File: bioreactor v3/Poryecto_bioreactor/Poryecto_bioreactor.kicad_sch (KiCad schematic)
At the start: 11 parts, among them J1 Screw_Terminal_01x02, U2 OKI-78SR-5/1.5-W36-C (L7805)

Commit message: Actualizacion
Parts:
- added C11: 100 nF, symbol Device:C
- added D2: 1N5819, Diode_THT:D_DO-41_SOD81_P10.16mm_Horizontal, symbol Diode:1N5819
- added J_BTN_NAV, J_BTN_ON, J_BTN_REG, J_BTN_RESET, J_MOTOR: PinHeader_1x02_P2.54mm_Vertical, symbol Connector_Generic:Conn_01x02
- added J_LCD: Conn_01x04_Pin, Connector_PinHeader_2.54mm:PinHeader_1x04_P2.54mm_Vertical, symbol Connector:Conn_01x04_Pin
- added J_RPM, J_TEMP: Conn_01x03, Connector_PinHeader_2.54mm:PinHeader_1x03_P2.54mm_Vertical, symbol Connector_Generic:Conn_01x03
- added Q1: IRLZ44N, Package_TO_SOT_THT:TO-220-3_Vertical, symbol Transistor_FET:IRLZ44N
- added R4: 10 kΩ, Package_TO_SOT_THT:TO-220-3_Vertical, symbol Device:R
- added R5: 4,7 kΩ, symbol Device:R
- added R6: 10 kΩ, symbol Device:R
- added R7: R, symbol Device:R
- R3: renamed from R1; value R -> 100 Ω
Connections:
- net +12V_PROT: now also C11.2, D2.1 (K), J_MOTOR.1 (Pin_1)
- net +5V: now also J_RPM.1 (Pin_1), J_TEMP.1 (Pin_1), R5.2, R6.2
- net GND: now also J_RPM.3 (Pin_3), J_TEMP.3 (Pin_3), Q1.3 (S), R4.1
- net BTN_NAV: now reaches A1.10 (D7)
- net BTN_NAV: now also J_BTN_NAV.1 (Pin_1)
- net ALARM_CTRL: now reaches A1.11 (D8)
- net ALARM_CTRL: now also R7.1
- net PWM_MOTOR: now reaches A1.12 (D9)
- net PWM_MOTOR: now also R3.1
- net SDA: now reaches A1.23 (A4)
- net SDA: now also J_LCD.3 (Pin_3)
- net SCL: now reaches A1.24 (A5)
- net SCL: now also J_LCD.4 (Pin_4)
- net RESET: now reaches A1.28 (~{RESET})
- net RESET: now also A1.3 (~{RESET}), J_BTN_RESET.1 (Pin_1)
- net RPM_SIGNAL: now reaches A1.5 (D2)
- net RPM_SIGNAL: now also J_RPM.2 (Pin_2), R6.1
- net TEMP_DATA: now reaches A1.7 (D4)
- net TEMP_DATA: now also J_TEMP.2 (Pin_2), R5.1
- net BTN_ON: now reaches A1.8 (D5)
- net BTN_ON: now also J_BTN_ON.1 (Pin_1)
- net BTN_REG: now reaches A1.9 (D6)
- net BTN_REG: now also J_BTN_REG.1 (Pin_1)
- net GATE_Q1: now reaches R3.2
- net GATE_Q1: now also Q1.1 (G), R4.2
- new net MOTOR-: C11.1, D2.2 (A), J_MOTOR.2 (Pin_2), Q1.2 (D)
- no-connect marks 3 -> 14
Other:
- note added: "18"
- note added: "19"
- note added: "20"
- note added: "21"
- note added: "22"
- note added: "23"
- note added: "24"
- note added: "25"
- note added: "26"
- note added: "27"
- note added: "28"
- note added: "29"
- note added: "30"
- note added: "31"
- note added: "32"
- note added: "33"
- note added: "34"
- note added: "35"
- note added: "36"
- note added: "37"
- note added: "38"
- note added: "39"
- note added: "Conector (bornera) para el sensor RPM"
- note added: "Conector (bornera) para el sensor de temperatura"
- note added: "Conector (bornera) para la pantalla"
- note added: "Conector para el botón de encendido"
- note added: "Todos los pines marcados con x no se ocuparán"
- note added: "conector del motor de 6 V"
- note removed: "VIN, 3V3, AREF no se usarán"
- moved on the sheet: R3

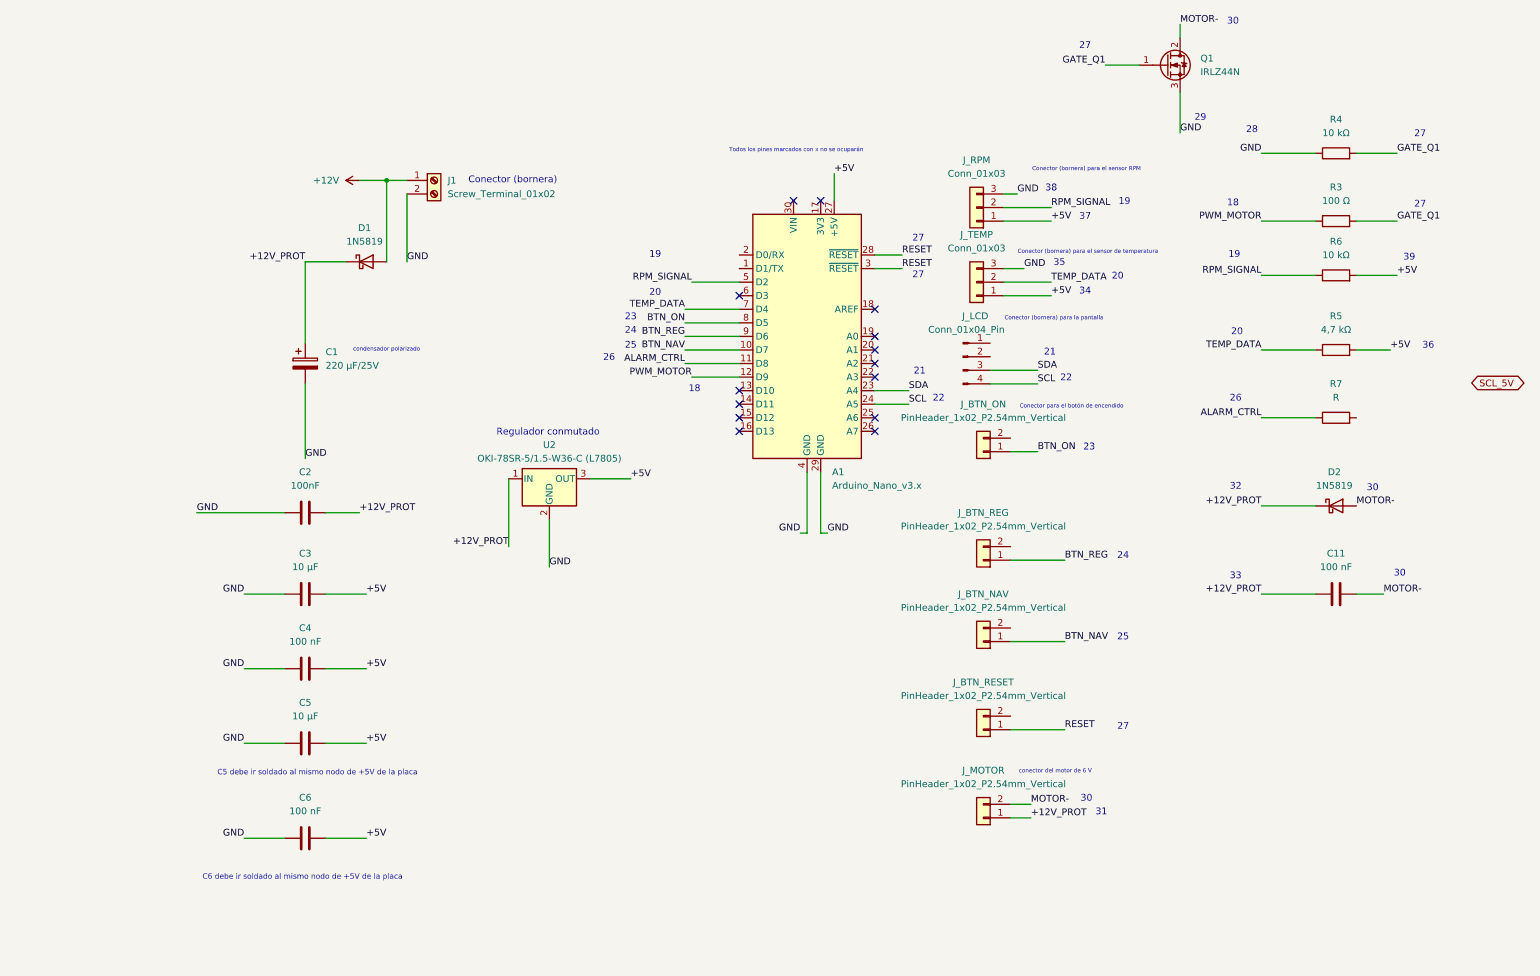
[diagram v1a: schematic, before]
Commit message: Esquemático terminado, generado de lista de componentes boom
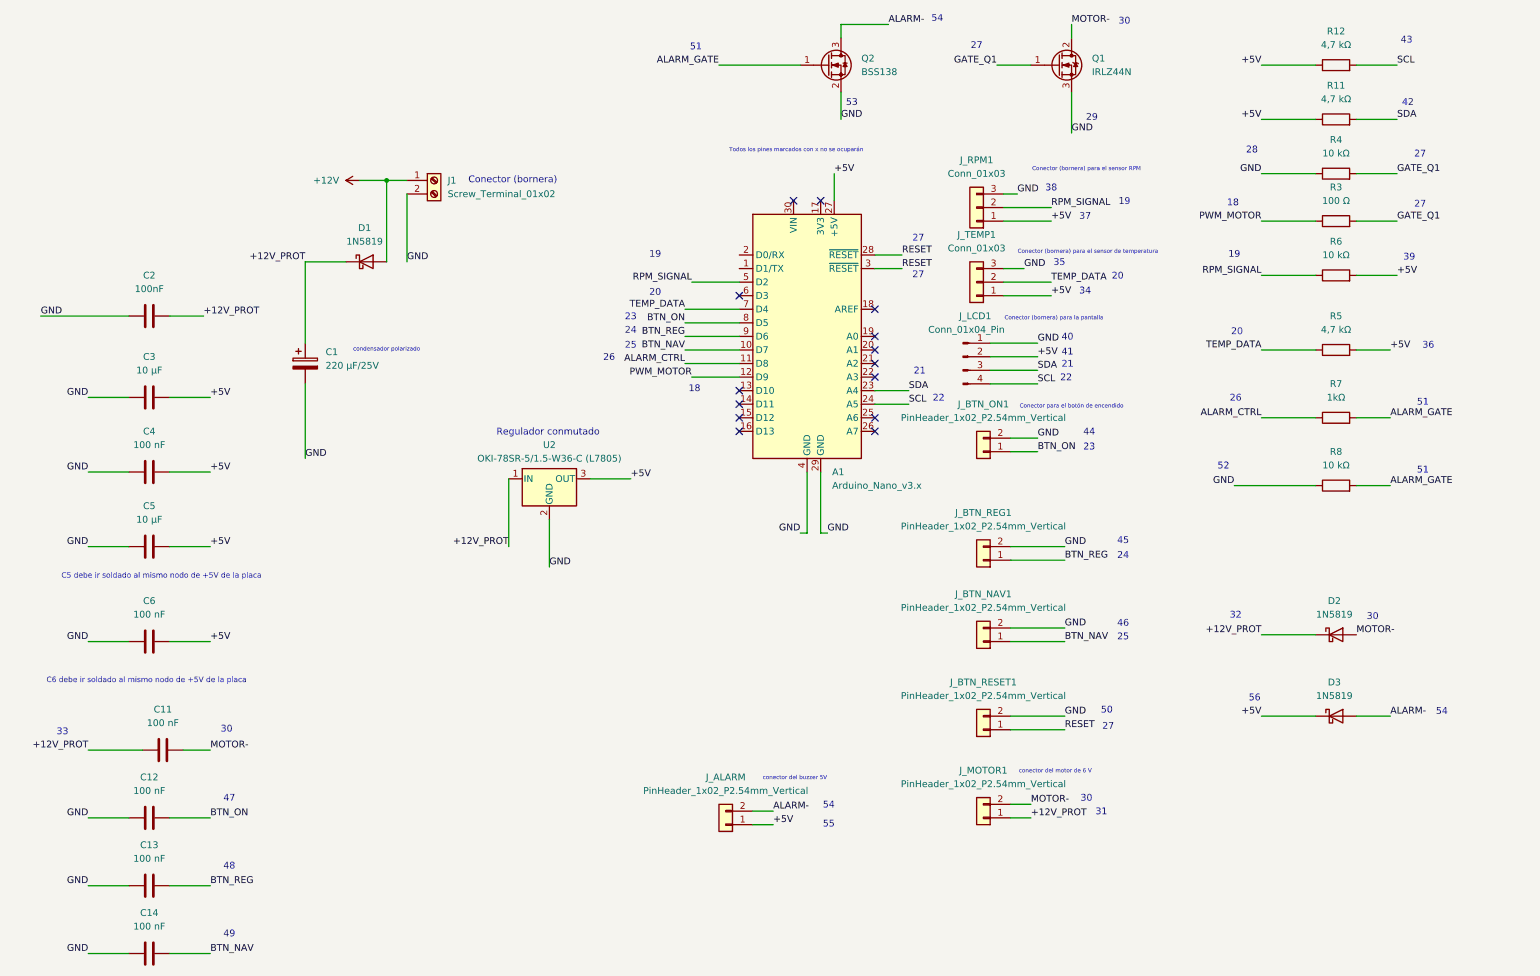
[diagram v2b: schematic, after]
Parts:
- added C12, C13, C14: 100 nF, symbol Device:C
- added D3: 1N5819, Diode_THT:D_DO-41_SOD81_P10.16mm_Horizontal, symbol Diode:1N5819
- added J_ALARM: PinHeader_1x02_P2.54mm_Vertical, symbol Connector_Generic:Conn_01x02
- added Q2: BSS138, Package_TO_SOT_SMD:SOT-23, symbol Transistor_FET:BSS138
- added R11, R12: 4,7 kΩ, Package_TO_SOT_THT:TO-220-3_Vertical, symbol Device:R
- added R8: 10 kΩ, symbol Device:R
- R7: value R -> 1kΩ
- renumbered J_BTN_NAV to J_BTN_NAV1, J_BTN_ON to J_BTN_ON1, J_BTN_REG to J_BTN_REG1, J_BTN_RESET to J_BTN_RESET1, J_LCD to J_LCD1, J_MOTOR to J_MOTOR1, J_RPM to J_RPM1, J_TEMP to J_TEMP1
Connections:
- net +5V: now also J_LCD1.2 (Pin_2), D3.1 (K), J_ALARM.1 (Pin_1), R11.1, R12.1
- net BTN_ON: now also C12.1
- net GND: now also J_BTN_NAV1.2 (Pin_2), J_BTN_ON1.2 (Pin_2), J_BTN_REG1.2 (Pin_2), J_BTN_RESET1.2 (Pin_2), J_LCD1.1 (Pin_1), C12.2, C13.2, C14.2, Q2.2 (S), R8.1
- net SCL: now also R12.2
- net SDA: now also R11.2
- net ALARM_GATE: now reaches R7.2
- net ALARM_GATE: now also Q2.1 (G), R8.2
- new net ALARM-: D3.2 (A), J_ALARM.2 (Pin_2), Q2.3 (D)
- new net BTN_NAV : C14.1
- new net BTN_REG : C13.1
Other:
- note added: "40"
- note added: "41"
- note added: "42"
- note added: "43"
- note added: "44"
- note added: "45"
- note added: "46"
- note added: "47"
- note added: "48"
- note added: "49"
- note added: "50"
- note added: "51"
- note added: "52"
- note added: "53"
- note added: "54"
- note added: "55"
- note added: "56"
- note added: "conector del buzzer 5V"
- moved on the sheet: C2, C3, C4, C5, C6, D2, Q1, R4

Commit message: actualizacion de esquemático
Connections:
- net +12V renamed +12V_IN
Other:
- note added: "1"
- note added: "10"
- note added: "11"
- note added: "12"
- note added: "14"
- note added: "2"
- note added: "3"
- note added: "4"
- note added: "5"
- note added: "6"
- note added: "7"
- note added: "8"
- note added: "9"
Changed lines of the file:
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@@
+		)
+	)
+	(text "14"
+		(exclude_from_sim no)
+		(at 169.926 113.538 0)
+		(effects
+			(font
+				(size 1.27 1.27)
+			)
+		)
+	)
+	(text "2"
+		(exclude_from_sim no)
+		(at 94.488 58.928 0)
+		(effects
+			(font
+				(size 1.27 1.27)
+			)
 		)
 	)
@@
 		)
 	)
+	(text "6"
+		(exclude_from_sim no)
+		(at 115.57 89.154 0)
+		(effects
+			(font
+				(size 1.27 1.27)
+			)
+		)
+	)
+	(text "7"
+		(exclude_from_sim no)
+		(at 117.602 113.792 0)
+		(effects
+			(font
+				(size 1.27 1.27)
+			)
+		)
+	)
+	(text "3"
+		(exclude_from_sim no)
+		(at 64.516 56.388 0)
+		(effects
+			(font
+				(size 1.27 1.27)
+			)
+		)
+	)
 	(text "Todos los pines marcados con x no se ocuparán"
 		(exclude_from_sim no)
@@
 		)
 	)
+	(text "1"
+		(exclude_from_sim no)
+		(at 119.38 46.99 0)
+		(effects
+			(font
+				(size 1.27 1.27)
+			)
+		)
+	)
 	(text "18"
 		(exclude_from_sim no)
@@
 		)
 	)
+	(text "8"
+		(exclude_from_sim no)
+		(at 136.398 99.568 0)
+		(effects
+			(font
+				(size 1.27 1.27)
+			)
+		)
+	)
 	(text "32"
 		(exclude_from_sim no)
@@
 		)
 	)
+	(text "4"
+		(exclude_from_sim no)
+		(at 75.184 74.422 0)
+		(effects
+			(font
+				(size 1.27 1.27)
+			)
+		)
+	)
 	(text "54"
 		(exclude_from_sim no)
@@
 		)
 	)
+	(text "5"
+		(exclude_from_sim no)
+		(at 40.64 59.944 0)
+		(effects
+			(font
+				(size 1.27 1.27)
+			)
+		)
+	)
 	(text "43"
 		(exclude_from_sim no)
@@
 		)
 	)
+	(text "4"
+		(exclude_from_sim no)
+		(at 72.136 93.472 0)
+		(effects
+			(font
+				(size 1.27 1.27)
+			)
+		)
+	)
+	(text "10"
+		(exclude_from_sim no)
+		(at 40.64 89.408 0)
+		(effects
+			(font
+				(size 1.27 1.27)
+			)
+		)
+	)
 	(text "26\n"
 		(exclude_from_sim no)
@@
 		)
 	)
+	(text "11"
+		(exclude_from_sim no)
+		(at 40.64 103.632 0)
+		(effects
+			(font
+				(size 1.27 1.27)
+			)
+		)
+	)
+	(text "14"
+		(exclude_from_sim no)
+		(at 160.782 113.284 0)
+		(effects
+			(font
+				(size 1.27 1.27)
+			)
+		)
+	)
 	(text "52"
 		(exclude_from_sim no)
@@
 		)
 	)
+	(text "12"
+		(exclude_from_sim no)
+		(at 40.64 121.158 0)
+		(effects
+			(font
+				(size 1.27 1.27)
+			)
+		)
+	)
 	(text "C5 debe ir soldado al mismo nodo de +5V de la placa"
 		(exclude_from_sim no)
@@
 		)
 	)
+	(text "9"
+		(exclude_from_sim no)
+		(at 40.894 75.438 0)
+		(effects
+			(font
+				(size 1.27 1.27)
+			)
+		)
+	)
 	(text "23"
 		(exclude_from_sim no)
@@
 		(exclude_from_sim no)
 		(at 184.912 80.264 0)
+		(effects
+			(font
+				(size 1.27 1.27)
+			)
+		)
+	)
+	(text "1"
+		(exclude_from_sim no)
+		(at 78.232 53.34 0)
 		(effects
 			(font
@@
 	(label "BTN_REG"
 		(at 140.97 73.66 180)
+		(effects
+			(font
+				(size 1.27 1.27)
+			)
+			(justify right bottom)
+		)
+	)
+	(label "+12V_IN"
+		(at 80.01 44.45 180)
 		(effects
 			(font
@@
 					(unit 1)
 				)
-			)
-		)
-	)
-	(symbol
-		(lib_id "power:+12V")
-		(at 80.01 44.45 90)
-		(unit 1)
-		(body_style 1)
-		(exclude_from_sim no)
-		(in_bom yes)
-		(on_board yes)
-		(in_pos_files yes)
-		(dnp no)
-		(fields_autoplaced yes)
-		(property "Reference" "#PWR01"
-			(at 83.82 44.45 0)
-			(hide yes)
-			(show_name no)
-			(do_not_autoplace no)
-			(effects
-				(font
-					(size 1.27 1.27)
-				)
-			)
-		)
-		(property "Value" "+12V"
-			(at 76.2 44.4499 90)
-			(show_name no)
-			(do_not_autoplace no)
-			(effects
-				(font
-					(size 1.27 1.27)
-				)
-				(justify left)
-			)
-		)
-		(property "Footprint" ""
-			(at 80.01 44.45 0)
-			(hide yes)
-			(show_name no)
-			(do_not_autoplace no)
-			(effects
-				(font
-					(size 1.27 1.27)
-				)
-			)
-		)
-		(property "Datasheet" ""
-			(at 80.01 44.45 0)
-			(hide yes)
-			(show_name no)
-			(do_not_autoplace no)
-			(effects
-				(font
-					(size 1.27 1.27)
-				)
-			)
-		)
-		(property "Description" "Power symbol creates a global label with name \"+12V\""
-			(at 80.01 44.45 0)
-			(hide yes)
-			(show_name no)
-			(do_not_autoplace no)
-			(effects
-				(font
-					(size 1.27 1.27)
-				)
-			)
-		)
-		(pin "1"
-		)
-		(instances
-			(project "Poryecto_bioreactor"
-				(path "/408c0b9b-6243-46a6-b02f-3125cc0037ea"
-					(reference "#PWR01")
-					(unit 1)
-				)
